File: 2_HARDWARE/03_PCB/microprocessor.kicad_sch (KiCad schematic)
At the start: 29 parts, among them SW1 TS-1187A-B-A-B, SW2 SS-12D02-VG4, SW3 SS-12D02-VG4, U11 STM32F446ZETx, Y1 32.768k

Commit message: MINOR: Changed Boot Select Switches to Pull-Downs / Pull Up DNI and continued layout.
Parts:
- removed SW2, SW3: SS-12D02-VG4, BRZK_SW:SW_TH_Slide_SPDT_Straight_SS-12D02-VG4, symbol BRZK_SWITCH:SS-12D02-VG4
- added R31, R33: 10k, Resistor_SMD:R_0603_1608Metric, symbol Device:R_Small_US
- renumbered R31 to R30, R33 to R34
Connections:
- net 3P3V_D: now also R31.2, R33.2
- net GND: now also R32.2, R34.2
- net GPIO_BOOT0_SW_MCU_3P3_L: now also R31.1
- net GPIO_BOOT1_SW_MCU_3P3_L: now also R33.1
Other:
- note added: "BOOT0 CONFIG PINS"
- note added: "BOOT1 CONFIG PINS"
- note removed: "BOOT0 SLIDE SWITCH"
- note removed: "BOOT1 SLIDE SWITCH"
- moved on the sheet: R34

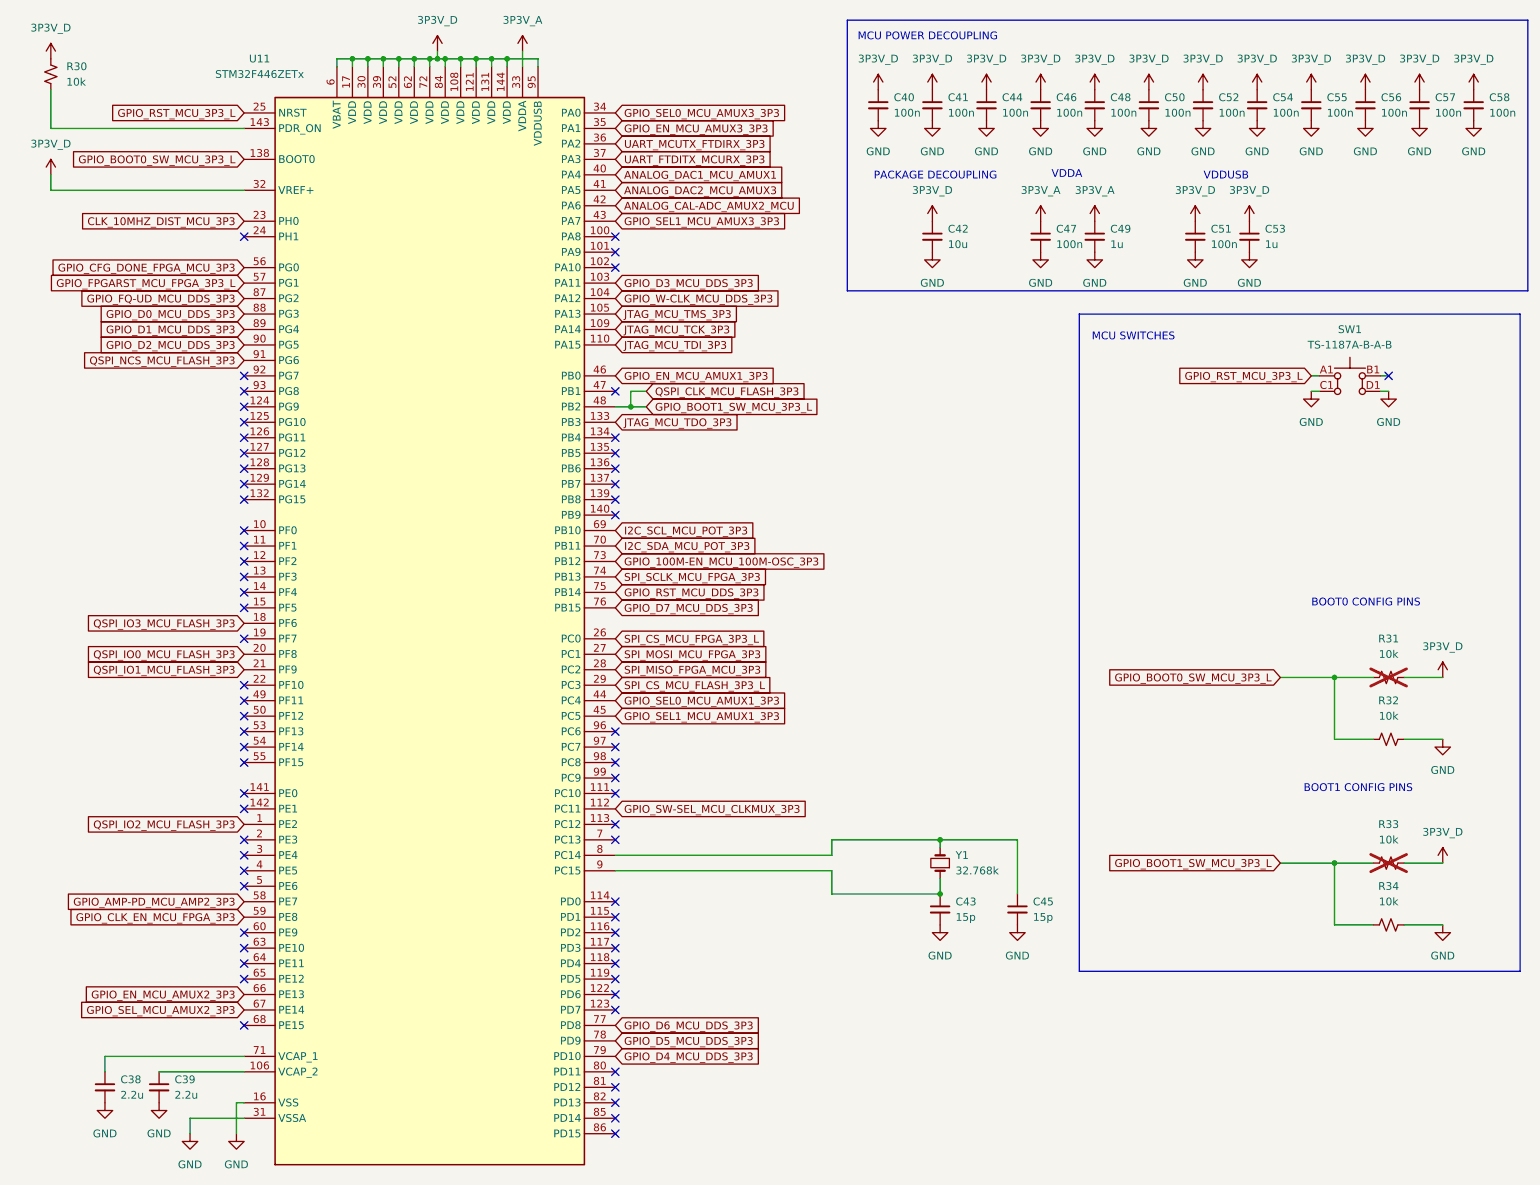
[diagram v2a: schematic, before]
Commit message: FEAT: Repinned the MCU to better support new layout.
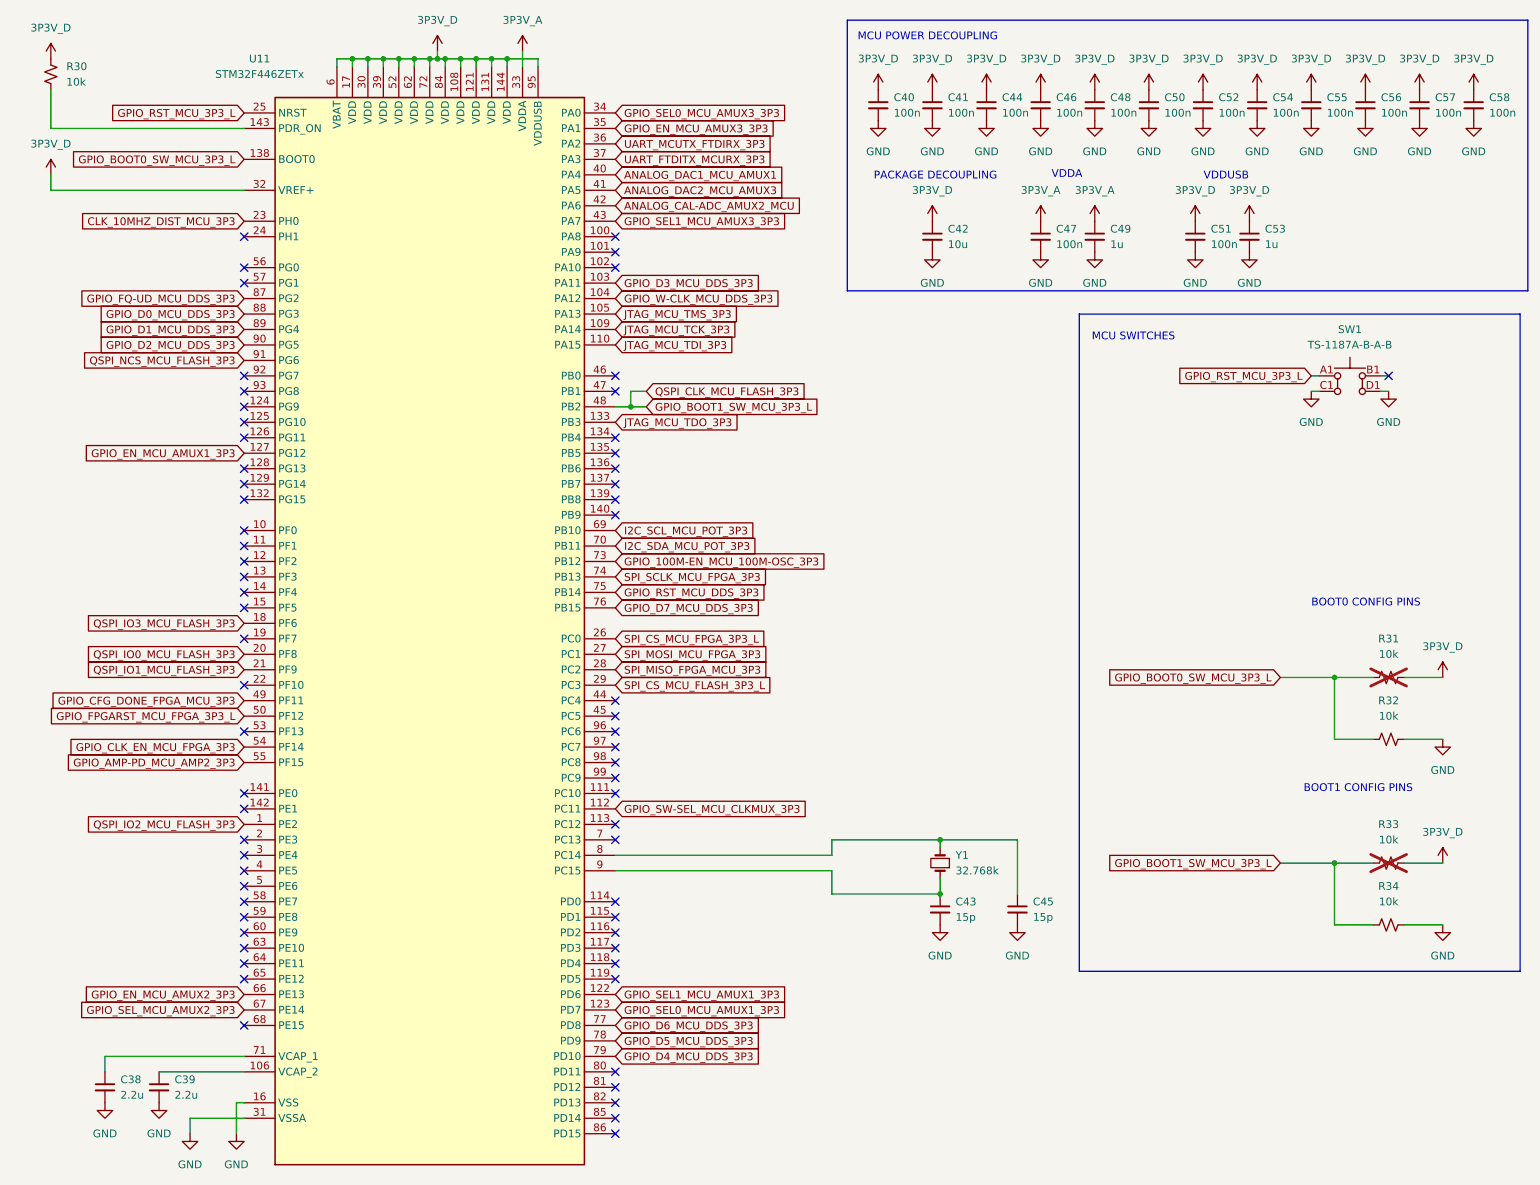
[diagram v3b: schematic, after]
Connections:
- net GPIO_AMP-PD_MCU_AMP2_3P3: now also U11.55 (PF15); no longer U11.58 (PE7)
- net GPIO_CFG_DONE_FPGA_MCU_3P3: now also U11.49 (PF11); no longer U11.56 (PG0)
- net GPIO_CLK_EN_MCU_FPGA_3P3: now also U11.54 (PF14); no longer U11.59 (PE8)
- net GPIO_EN_MCU_AMUX1_3P3: now also U11.127 (PG12); no longer U11.46 (PB0)
- net GPIO_FPGARST_MCU_FPGA_3P3_L: now also U11.50 (PF12); no longer U11.57 (PG1)
- net GPIO_SEL0_MCU_AMUX1_3P3: now also U11.123 (PD7); no longer U11.44 (PC4)
- net GPIO_SEL1_MCU_AMUX1_3P3: now also U11.122 (PD6); no longer U11.45 (PC5)

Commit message: FEAT: Routed FPGA to DDS and FPGA to MCU Signals.
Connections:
- net 3P3V_D: now also R33.1; no longer R33.2
- net GND: now also R34.1; no longer R34.2
- net GPIO_BOOT1_SW_MCU_3P3_L: now also R33.2, R34.2; no longer R33.1, R34.1
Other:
- moved on the sheet: R33, R34
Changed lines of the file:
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@@
 	(symbol
 		(lib_id "Device:R_Small_US")
-		(at 238.76 152.4 90)
+		(at 238.76 152.4 270)
+		(mirror x)
 		(unit 1)
 		(exclude_from_sim no)
@@
 	(symbol
 		(lib_id "Device:R_Small_US")
-		(at 238.76 162.56 90)
+		(at 238.76 162.56 270)
+		(mirror x)
 		(unit 1)
 		(exclude_from_sim no)
